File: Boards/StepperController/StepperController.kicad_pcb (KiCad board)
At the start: 2 copper layers, 160 x 100 mm, 206 parts, among them IC1 ATMEGA128-A, J1 Jog, J2 SPI_Extern, J4 Reference, J5 Display, J6 Ext, J7 Spindle, P1 Power, P10 CONN_Z, P11 Buttons, P2 Cover, P3 USB_B, P4 Relay2, P5 Relay1, P6 Emer_Off, P7 JTAG, P8 CONN_X, P9 CONN_Y, Q1 BC817-40, Q2 BC817-40, Q3 BC817-40, Q4 BC817-40, Q5 BC817-40, Q6 BC807-40, Q7 BC807-40, Q8 BC817-40, Q9 BC817-40, SW1 ResetCycle, U1 LM2576S-5, U10 74HC245, U11 74HC245, U2 74HC11, U3 FT232RL, U4 74LS11, U5 TMC2660, U6 TMC2660, U7 TMC2660, U8 74HC245, U9 74HC245, X1 16MHz, Y1 16MHz

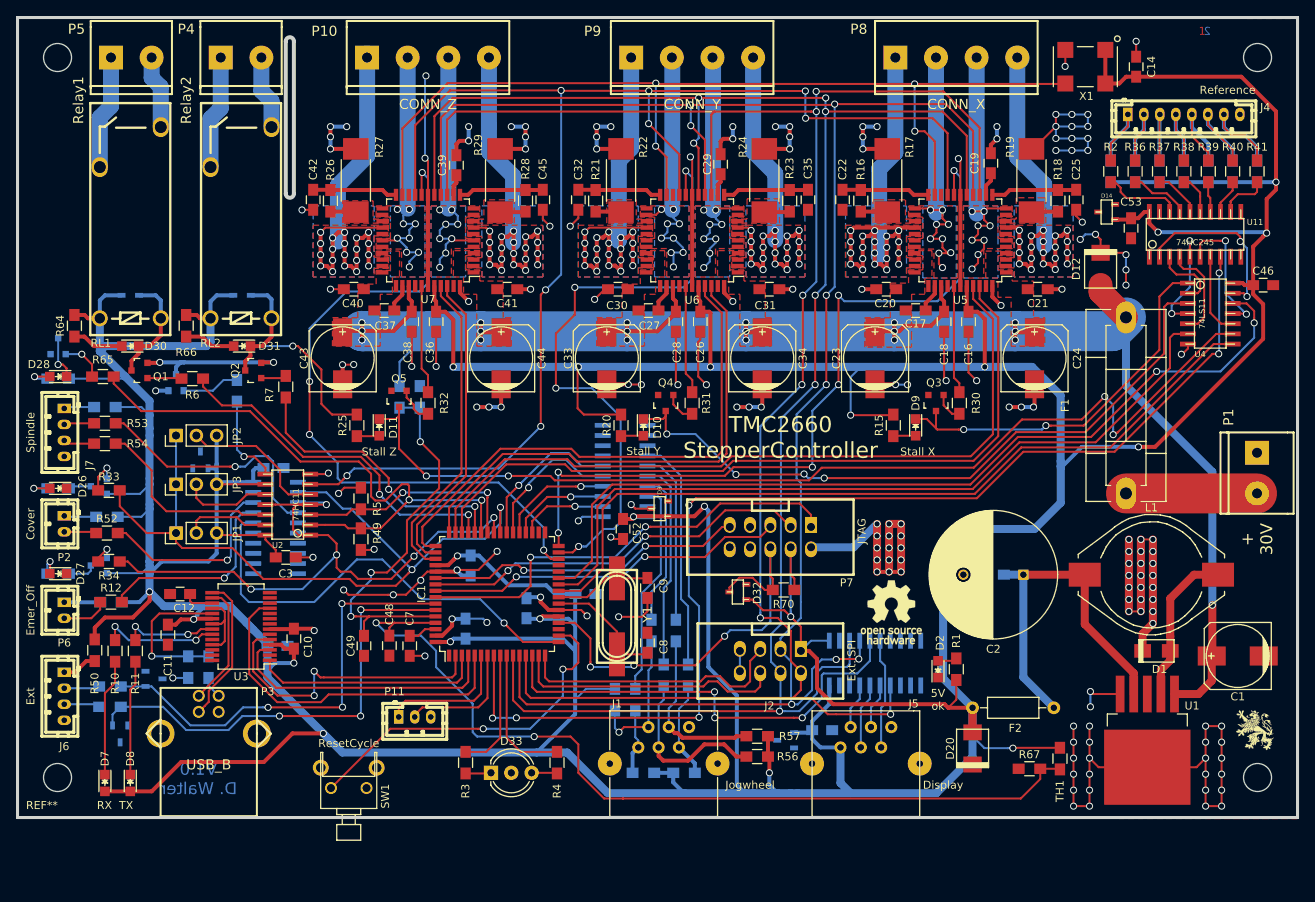
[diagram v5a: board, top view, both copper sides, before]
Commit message: Added Buffers for I/O, Changed Pinout to be compatible with grbl
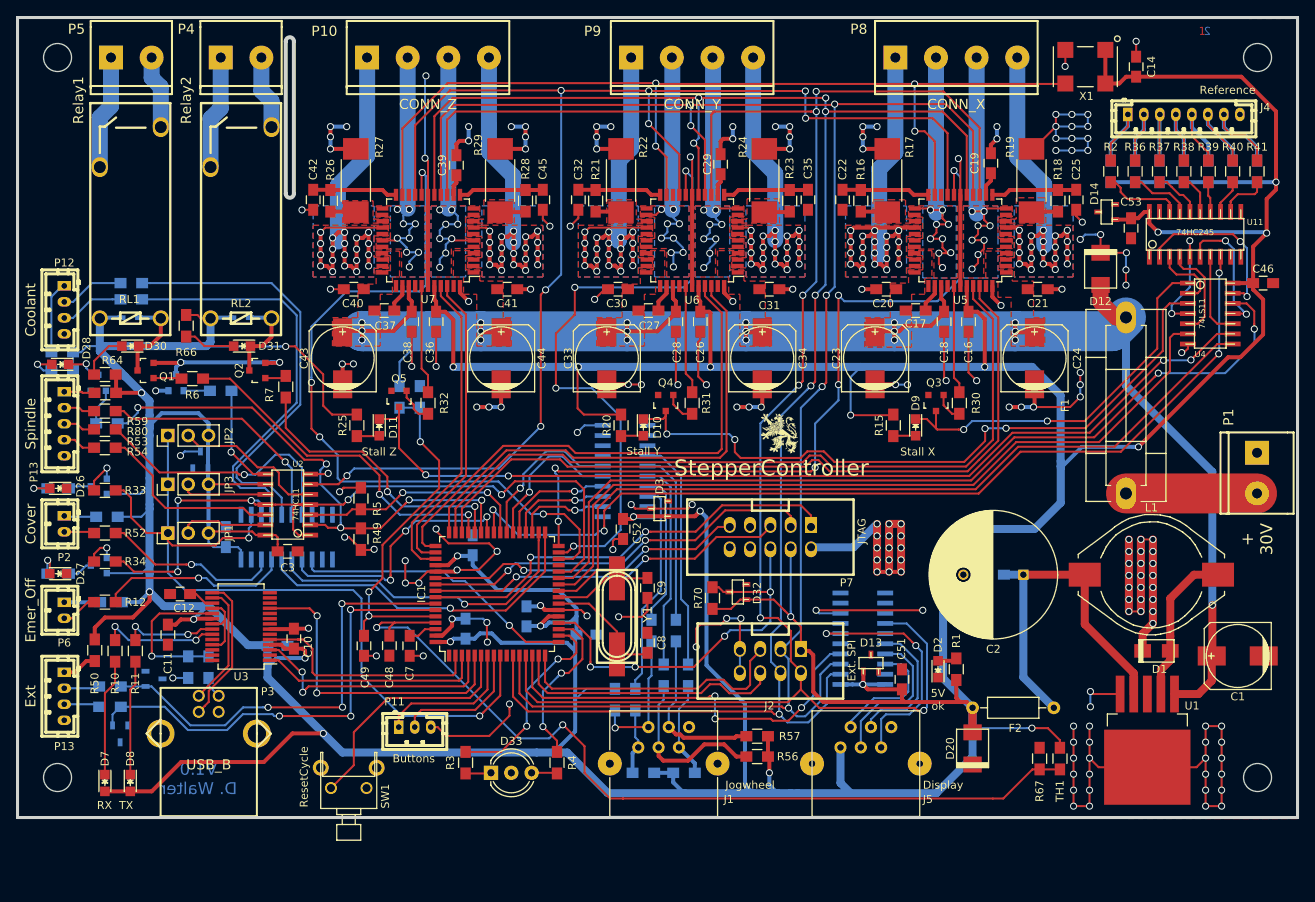
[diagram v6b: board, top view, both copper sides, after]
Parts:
- removed J7: Spindle, w_conn_jst-ph:b4b-ph-kl
- removed REF***: OSHW-Logo_7.5x8mm_SilkScreen, Symbols:OSHW-Logo_7.5x8mm_SilkScreen
- added P12: Coolant, w_conn_jst-ph:b4b-ph-kl, F.Cu at (69.8, 89.5)
- added P13: Spindle, w_conn_jst-ph:b5b-ph-kl, F.Cu at (69.8, 103.7)
- added R77: 10R, Resistors_SMD:R_0805_HandSoldering, B.Cu at (69.6, 94.7)
- added R78: 100R, Resistors_SMD:R_0805_HandSoldering, B.Cu at (78.2, 88.1)
- added R79: 100R, Resistors_SMD:R_0805_HandSoldering, B.Cu at (78.2, 86.1)
- added R80: 100R, Resistors_SMD:R_0805_HandSoldering, F.Cu at (74.9, 102.1)
- C51, D13, R59: moved to F.Cu
- R65: moved to B.Cu
- moved G*** 70.1 mm to (159.3, 104.9)
- moved D13 14.4 mm to (170.7, 133.6), turned to 0 degrees
- moved C51 11.8 mm to (174.6, 135.6), turned to 90 degrees
- moved C50 10.5 mm to (90.0, 117.9), turned to 90 degrees
- moved R70 8.95 mm to (150.9, 125.5), turned to 90 degrees
- moved R64 7.19 mm to (74.9, 97.5), turned to 180 degrees
- moved Q8 6.80 mm to (74.1, 98.6)
- moved R65 5.86 mm to (75.2, 103.6)
- moved C47 5.08 mm to (135.1, 130.0)
- moved U9 3.41 mm to (169.7, 130.6), turned to 90 degrees
- moved D6 2.80 mm to (91.9, 90.4)
- moved D5 2.79 mm to (78.1, 90.4)
- moved C6 2.55 mm to (120.9, 118.9), turned to 90 degrees
- moved R35 2.03 mm to (89.4, 99.6), turned to 0 degrees
- moved U10 1.81 mm to (97.7, 117.9), turned to 0 degrees
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- renumbered J6 to P13
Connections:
- IC1 pad 10: /Controller/LED2 -> (no net)
- IC1 pad 18: Net-(IC1-Pad18) -> /Controller/LED1
- IC1 pad 19: (no net) -> /Controller/LED2
- IC1 pad 28: (no net) -> /Controller/Emergency_Off
- IC1 pad 33: (no net) -> /Controller/Cool_Flood
- IC1 pad 34: (no net) -> /Controller/Cool_Mist
- IC1 pad 40: /Controller/Cover -> /Controller/Enable
- IC1 pad 41: /Controller/Emergency_Off -> /Interface/Ref_T1
- IC1 pad 42: /Controller/Enable -> /Controller/Spindle_Dir
- IC1 pad 6: /Controller/FeedHold -> Net-(IC1-Pad6)
- IC1 pad 8: /Interface/Ref_T1 -> /Controller/FeedHold
- IC1 pad 9: /Controller/LED1 -> /Controller/Cover
- P11 pad 1: /Controller/FeedHold -> /Controller/CycleStart
- P11 pad 2: /Controller/CycleStart -> /Controller/FeedHold
- P3 pad : (no net) -> GND
- SW1 pad 1: Net-(IC1-Pad18) -> Net-(IC1-Pad6)
- SW1 pad 3: (no net) -> GND
- U10 pad 13: GND -> /Controller/Spindle_PWM
- U10 pad 14: GND -> /Controller/Spindle_Dir
- U10 pad 15: GND -> /Controller/Cool_Mist
- U10 pad 16: /Controller/Spindle_PWM -> /Controller/Cool_Flood
- U10 pad 4: Net-(R53-Pad1) -> Net-(R78-Pad1)
- U10 pad 5: (no net) -> Net-(R79-Pad1)
- U10 pad 6: (no net) -> Net-(R80-Pad1)
- U10 pad 7: (no net) -> Net-(R53-Pad1)
- U9 pad 15: Net-(J5-Pad4) -> (no net)
- U9 pad 16: Net-(J5-Pad3) -> Net-(J5-Pad4)
- U9 pad 17: Net-(J5-Pad2) -> Net-(J5-Pad3)
- U9 pad 18: (no net) -> Net-(J5-Pad2)
- U9 pad 2: GND -> /Controller/SCK
- U9 pad 3: /Controller/SCK -> /Controller/SDI
- U9 pad 4: /Controller/SDI -> /Interface/CS_Disp
- U9 pad 5: /Interface/CS_Disp -> GND
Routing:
- net GND: track 470.4 -> 535.9 mm, vias 168 -> 182
- net Net-(R79-Pad1): track 0.00 -> 54.1 mm
- net Net-(R78-Pad1): track 0.00 -> 52.2 mm
- net Net-(IC1-Pad18): track 44.6 -> 0.00 mm, vias 2 -> 0
- net /Controller/Cool_Flood: track 0.00 -> 43.2 mm, vias 0 -> 1
- net /Controller/Cool_Mist: track 0.00 -> 40.5 mm, vias 0 -> 1
- net /Controller/Spindle_Dir: track 0.00 -> 32.7 mm, vias 0 -> 3
- net Net-(R80-Pad1): track 0.00 -> 30.8 mm, vias 0 -> 1
- net Net-(IC1-Pad6): track 0.00 -> 30.3 mm
- net /Interface/Ref_T1: track 147.1 -> 118.0 mm, vias 6 -> 4
- net /Controller/Spindle_PWM: track 56.9 -> 35.8 mm
- net Net-(J5-Pad5): track 13.8 -> 30.5 mm, vias 0 -> 2
- net /Controller/SDO: track 234.9 -> 249.5 mm
- net /Controller/Emergency_Off: track 81.0 -> 93.5 mm
- net Net-(J5-Pad4): track 5.68 -> 17.9 mm
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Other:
- board text added: "Buttons"
- board text added: "Dir"
- board text added: "Flood"
- board text added: "Mist"
- board text added: "Motor"
- board text added: "No Check"
- board text added: "StepperController"
- board text removed: "Ignore Cover"
- board text removed: "Steppers"
- board text removed: "TMC2660 StepperController"

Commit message: Changed Footprints
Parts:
- removed the P13 at (69.8, 137.7)
- added J6: Ext, w_conn_jst-ph:b4b-ph-kl, F.Cu at (69.8, 137.7)
- C51: moved to B.Cu
- D13, D14, D24, D25, D3, D32, D4: footprint w_smd_trans:sot23 -> Diodes_SMD:D_SOT-23_ANK
- U10, U11, U8, U9: footprint SO20:so-20 -> w_smd_dil:tssop-20
- moved C51 6.46 mm to (168.1, 136.4), turned to 0 degrees
- moved R57 4.68 mm to (159.5, 146.3), turned to 90 degrees
- moved D13 4.02 mm to (166.9, 134.9), turned to 270 degrees
- moved D14 2.51 mm to (201.9, 79.0), turned to 0 degrees
- moved C50 2.16 mm to (92.2, 117.9)
- moved C53 1.70 mm to (204.7, 80.0)
- moved U8 1.55 mm to (139.7, 111.1)
- moved R71 1.31 mm to (146.7, 148.5), turned to 90 degrees
- moved U9 1.27 mm to (169.7, 131.8)
- moved R13 1.14 mm to (142.2, 148.5), turned to 90 degrees
- moved R56 1.14 mm to (157.0, 146.3), turned to 90 degrees
- moved D24 0.82 mm to (80.3, 135.4), turned to 270 degrees
- moved U10 0.77 mm to (96.9, 117.9)
- moved U11 0.71 mm to (210.5, 80.0)
- moved D32 0.63 mm to (154.4, 125.2), turned to 180 degrees
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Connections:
- P3 pad : GND -> (no net)
- SW1 pad 3: GND -> (no net)
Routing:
- net GND: track 535.9 -> 557.2 mm, vias 182 -> 181
- net (no net): track 0.00 -> 13.3 mm, vias 0 -> 2
- net +5V: track 906.0 -> 897.0 mm
- net Net-(J1-Pad4): track 21.4 -> 28.9 mm
- net Net-(R53-Pad1): track 33.2 -> 29.8 mm
- net /Controller/Emergency_Off: track 93.5 -> 96.8 mm
- net Net-(R41-Pad1): track 6.34 -> 9.01 mm
- net /Controller/Spindle_PWM: track 35.8 -> 38.0 mm
- net /Controller/Ref_X1: track 21.4 -> 19.3 mm
- net /Controller/SDO: track 249.5 -> 247.4 mm
- net Net-(R40-Pad1): track 4.36 -> 6.36 mm
- net Net-(R76-Pad1): track 29.2 -> 27.2 mm
- net Net-(J5-Pad5): track 30.5 -> 28.7 mm
- net /Controller/Ref_Y2: track 15.5 -> 13.7 mm
- net /Controller/Spindle_Dir: track 32.7 -> 34.4 mm
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
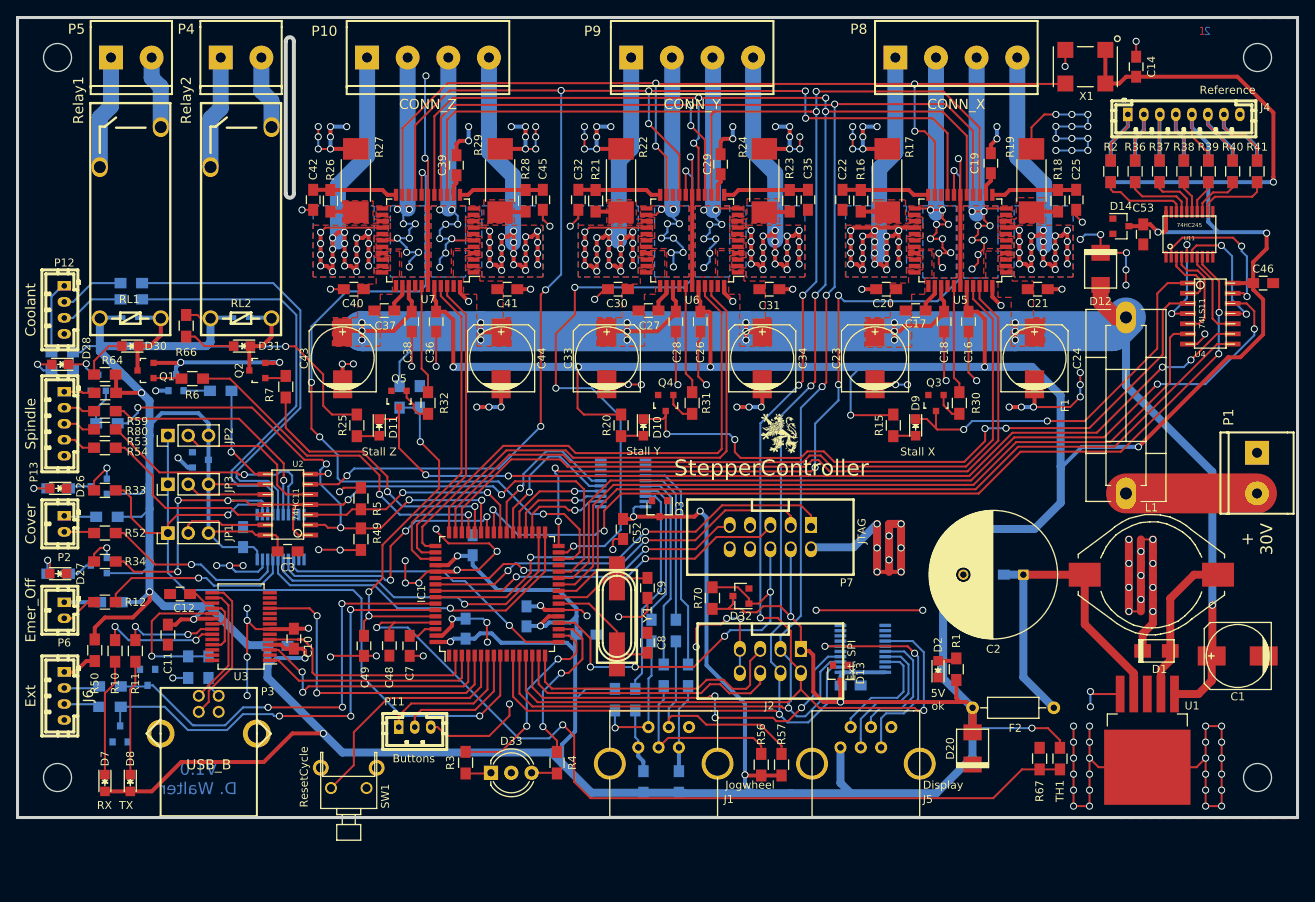
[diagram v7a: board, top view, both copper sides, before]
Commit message: Removed SW, Added HandController, Small PCB changes
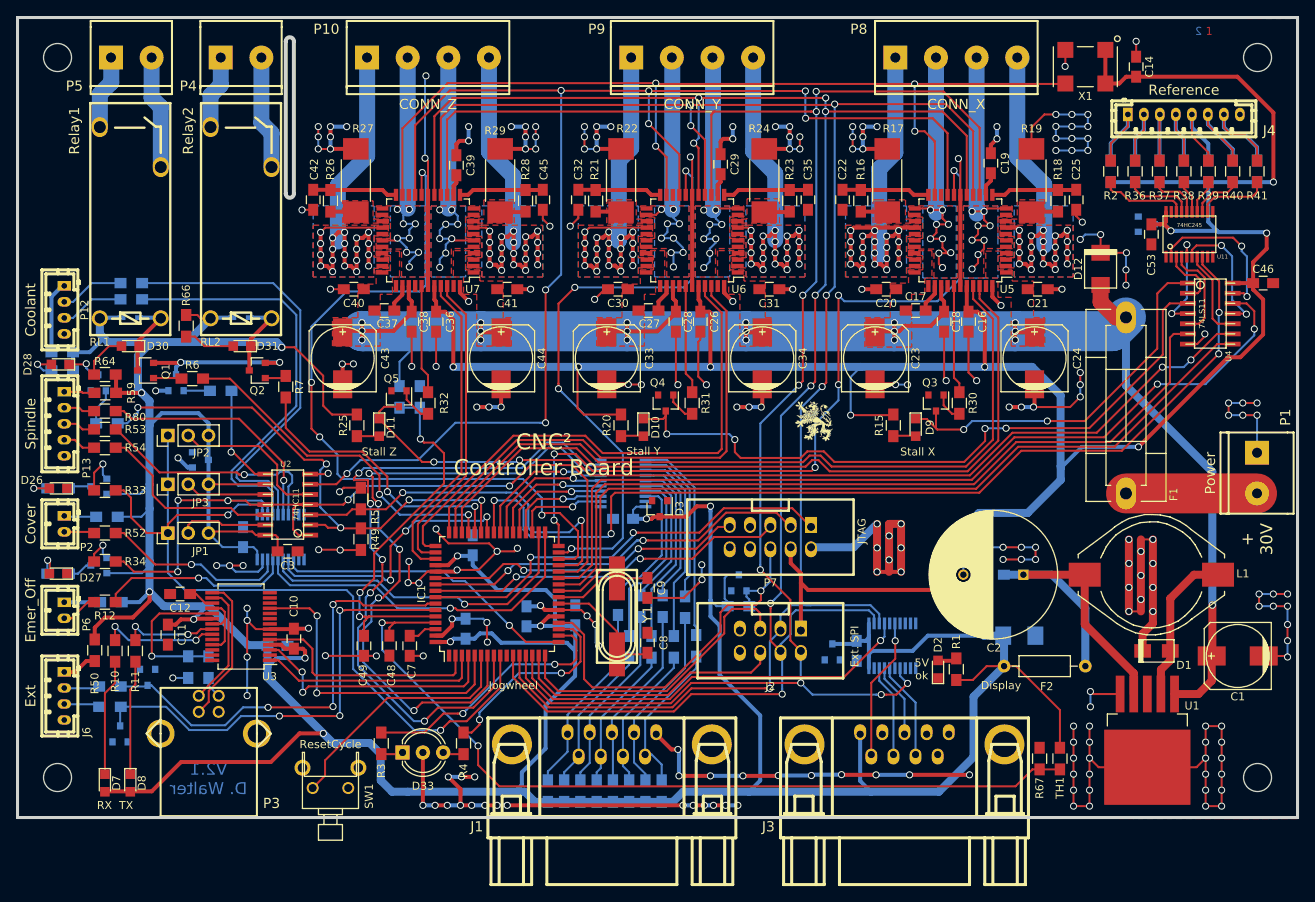
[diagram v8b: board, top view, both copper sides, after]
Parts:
- removed J5: Display, Connect:RJ12_E
- removed P11: Buttons, w_conn_jst-ph:b3b-ph-kl
- added J3: DB9_Female, w_conn_d-sub:DB_9F, F.Cu at (174.9, 150.9)
- added R81: 100R, Resistors_SMD:R_0805_HandSoldering, B.Cu at (146.1, 131.6)
- added R82: 100R, Resistors_SMD:R_0805_HandSoldering, B.Cu at (147.4, 126.6)
- added R83: 4k7, Resistors_SMD:R_0805_HandSoldering, B.Cu at (140.5, 149.6)
- added R84: 4k7, Resistors_SMD:R_0805_HandSoldering, B.Cu at (142.5, 149.6)
- added R85: 100R, Resistors_SMD:R_0805_HandSoldering, B.Cu at (148.8, 131.4)
- added R86: 4k7, Resistors_SMD:R_0805_HandSoldering, B.Cu at (144.5, 149.6)
- C52, D13, D14, D20, D32, R56, R57, R70: moved to B.Cu
- J1: value Jog -> DB9_Female; footprint Connect:RJ12_E -> w_conn_d-sub:DB_9F
- moved R57 23.3 mm to (136.4, 149.6)
- moved R56 22.8 mm to (134.4, 149.6)
- moved D20 15.3 mm to (189.2, 130.2), turned to 0 degrees
- moved R51 13.1 mm to (132.3, 149.6), turned to 90 degrees
- moved R72 12.1 mm to (139.1, 126.2)
- moved R13 12.0 mm to (130.3, 149.6)
- moved R4 11.9 mm to (119.8, 143.6)
- moved D33 11.3 mm to (112.1, 144.8)
- moved R3 10.8 mm to (109.5, 143.6)
- moved R76 9.20 mm to (144.7, 126.5)
- moved R74 9.12 mm to (141.9, 126.5)
- moved R71 8.33 mm to (138.4, 149.6)
- moved J1 7.50 mm to (138.3, 150.9)
- moved F2 6.53 mm to (197.5, 134.0)
- moved G*** 4.58 mm to (163.6, 103.4)
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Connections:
- IC1 pad 29: (no net) -> /Controller/Enable
- IC1 pad 37: /Controller/JogX -> /Controller/JogC
- IC1 pad 38: /Controller/JogY -> /Controller/JogX
- IC1 pad 39: /Controller/JogZ -> /Controller/JogY
- IC1 pad 40: /Controller/Enable -> /Controller/JogZ
- IC1 pad 7: /Controller/CycleStart -> /Controller/FeedHold
- IC1 pad 8: /Controller/FeedHold -> /Controller/CycleStart
- J1 pad 1: Net-(J1-Pad1) -> GND
- J1 pad 6: GND -> Net-(J1-Pad6)
- J1 pad 7: GND -> Net-(J1-Pad7)
- J1 pad 8: GND -> Net-(J1-Pad8)
- R13 pad 2: Net-(J1-Pad1) -> Net-(J1-Pad5)
- R51 pad 2: Net-(J1-Pad2) -> Net-(J1-Pad9)
- R56 pad 2: Net-(J1-Pad3) -> Net-(J1-Pad4)
- R57 pad 2: Net-(J1-Pad4) -> Net-(J1-Pad8)
- R71 pad 2: Net-(J1-Pad5) -> Net-(J1-Pad3)
- R72 pad 2: Net-(J1-Pad1) -> Net-(J1-Pad5)
- R73 pad 2: Net-(J1-Pad2) -> Net-(J1-Pad9)
- R74 pad 2: Net-(J1-Pad3) -> Net-(J1-Pad4)
- R75 pad 2: Net-(J1-Pad4) -> Net-(J1-Pad8)
- R76 pad 2: Net-(J1-Pad5) -> Net-(J1-Pad3)
- RL1 pad 11: Net-(P5-Pad1) -> Net-(P5-Pad2)
- RL1 pad 14: Net-(P5-Pad2) -> Net-(P5-Pad1)
- RL2 pad 11: Net-(P4-Pad1) -> Net-(P4-Pad2)
- RL2 pad 14: Net-(P4-Pad2) -> Net-(P4-Pad1)
- U8 pad 11: GND -> Net-(R85-Pad1)
- U8 pad 12: GND -> Net-(R82-Pad1)
- U8 pad 13: GND -> Net-(R81-Pad1)
- U8 pad 4: /Controller/JogX -> /Controller/JogC
- U8 pad 5: /Controller/JogY -> /Controller/JogX
- U8 pad 6: /Controller/JogZ -> /Controller/JogY
- U8 pad 7: (no net) -> /Controller/JogZ
- U8 pad 8: (no net) -> /Controller/FeedHold
- U8 pad 9: (no net) -> /Controller/CycleStart
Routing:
- net GND: track 557.2 -> 684.2 mm, vias 181 -> 228
- net /Controller/CycleStart: track 18.1 -> 86.6 mm, vias 0 -> 5
- net /Controller/FeedHold: track 17.0 -> 81.9 mm, vias 0 -> 5
- net Net-(R85-Pad1): track 0.00 -> 26.1 mm
- net Net-(R81-Pad1): track 0.00 -> 24.8 mm
- net Net-(R82-Pad1): track 0.00 -> 20.5 mm
- net Net-(J1-Pad6): track 0.00 -> 19.5 mm
- net Net-(J1-Pad9): track 0.00 -> 18.7 mm
- net /Controller/Enable: track 29.0 -> 47.7 mm
- net Net-(J1-Pad7): track 0.00 -> 18.6 mm
- net Net-(J1-Pad8): track 0.00 -> 18.2 mm
- net /Controller/SDO: track 247.4 -> 233.1 mm, vias 6 -> 8
- net /Controller/JogC: track 0.00 -> 14.0 mm, vias 0 -> 1
- net (no net): track 13.3 -> 0.00 mm, vias 2 -> 0
- net Net-(J1-Pad5): track 11.3 -> 24.3 mm
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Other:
- board text added: "CNC² Controller Board"
- board text added: "V2.1 D. Walter"
- board text removed: "Buttons"
- board text removed: "CycleStart"
- board text removed: "FeedHold"
- board text removed: "StepperController"
- board text removed: "V1.0 D. Walter"
